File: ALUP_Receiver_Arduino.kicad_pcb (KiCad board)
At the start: 2 copper layers, 50 x 45 mm, 9 parts, among them J1 Barrel_Jack_Switch, J2 5V LED, J3 D+ LED, J4 GND LED, U1 6N137

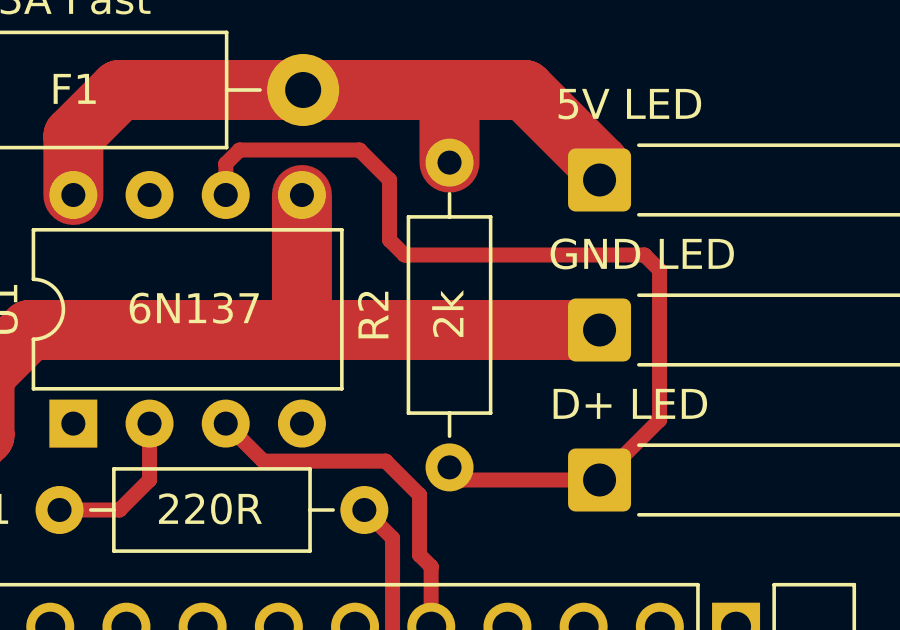
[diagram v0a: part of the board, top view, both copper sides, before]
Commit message: Change pullup resistor
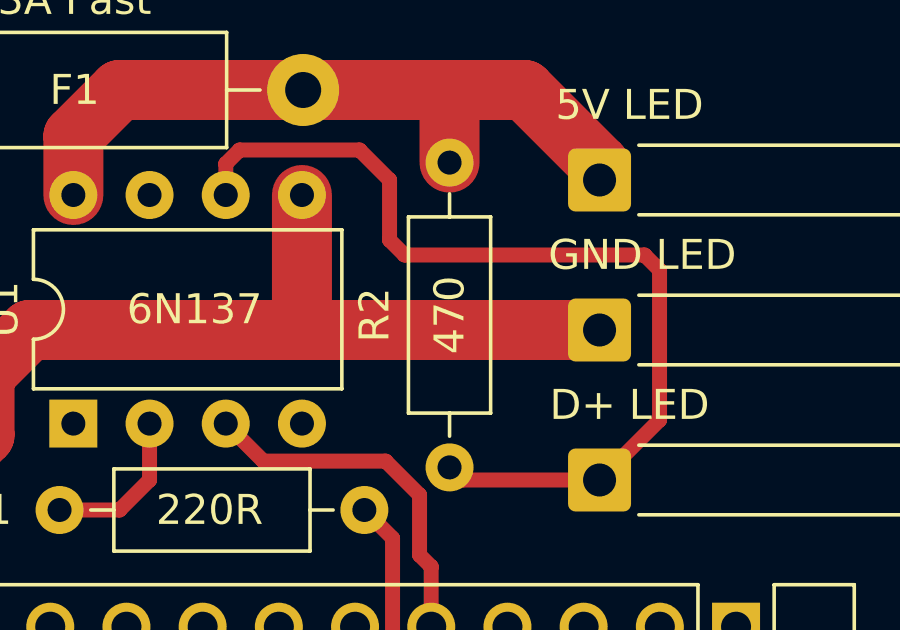
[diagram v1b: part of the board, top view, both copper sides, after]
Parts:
- R2: value 2k -> 470
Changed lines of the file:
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@@
 			)
 		)
-		(property "Value" "2k"
+		(property "Value" "470"
 			(at 5.08 0 -90)
 			(layer "F.SilkS")
